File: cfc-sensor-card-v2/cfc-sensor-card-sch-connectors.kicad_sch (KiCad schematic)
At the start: 4 parts, among them J1 J-SAMTEC-TFM-120-01-L-D-RA, J3 J-SAMTEC-TFM-110-01-L-D-RA

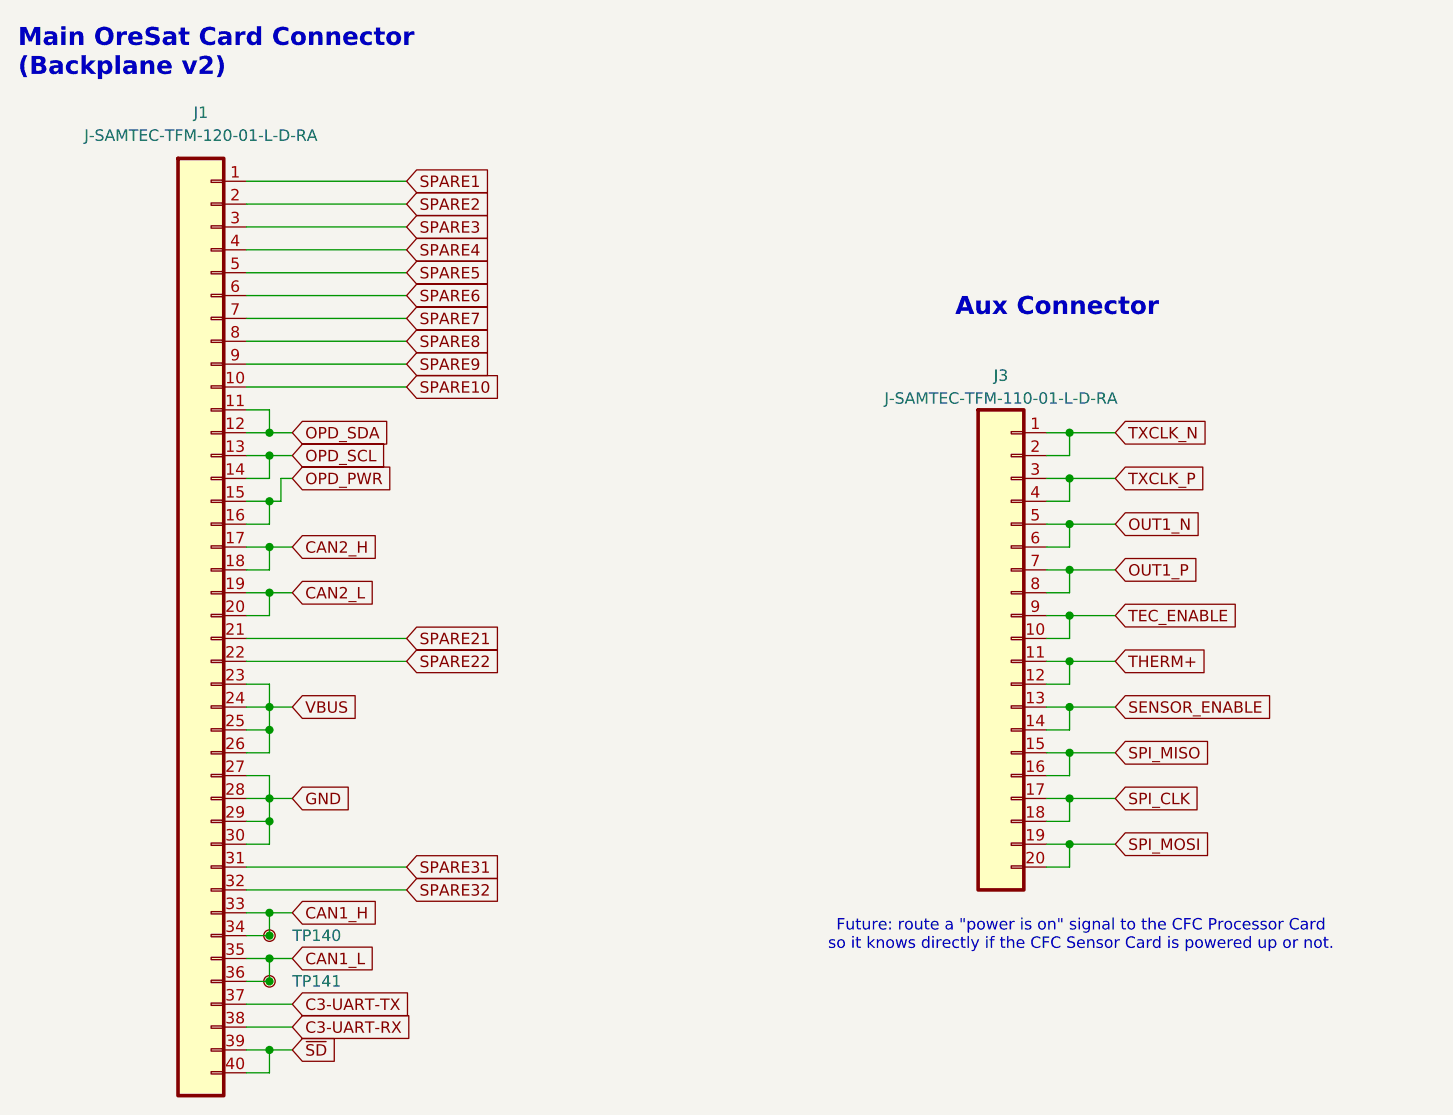
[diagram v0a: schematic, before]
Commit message: Fix and complete BOM, fix lots of little layout issue and footprint inconsistancies, and polish. Ready to go!
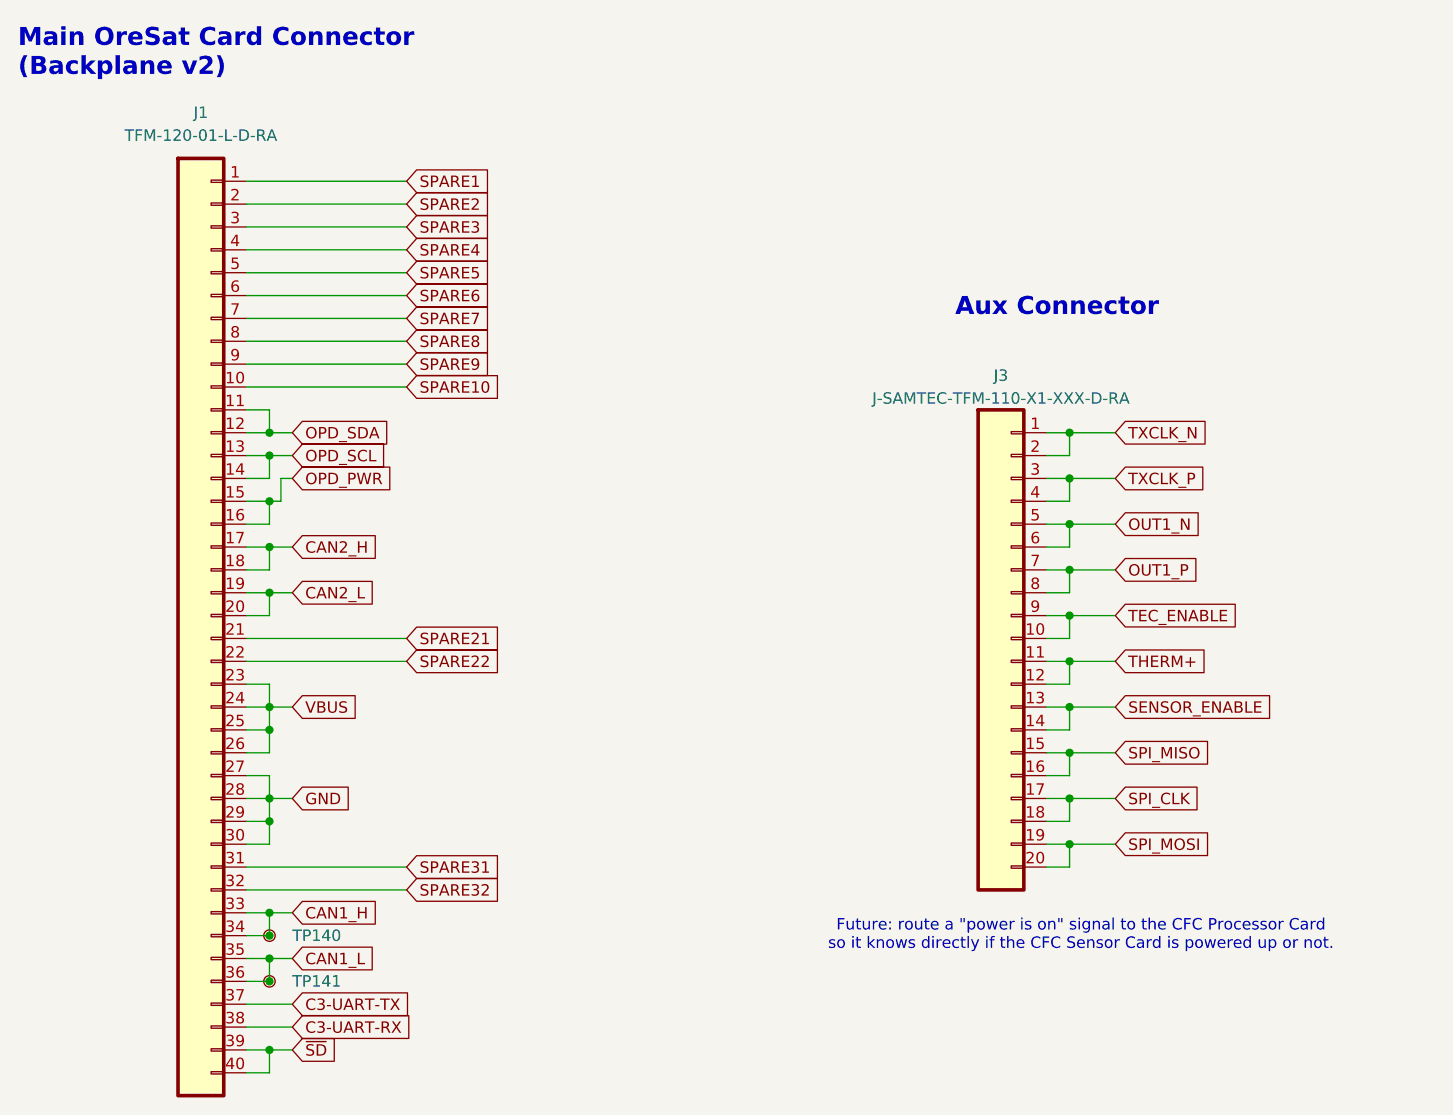
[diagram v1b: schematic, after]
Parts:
- J1: value J-SAMTEC-TFM-120-01-L-D-RA -> TFM-120-01-L-D-RA; DIS (none) -> DigiKey; DPN (none) -> SAM10145-ND; MFR (none) -> Samtec; MPN (none) -> TFM-120-01-L-D-RA
- J3: value J-SAMTEC-TFM-110-01-L-D-RA -> J-SAMTEC-TFM-110-X1-XXX-D-RA; DIS (none) -> Digikey; DPN (none) -> SAM10113-ND; MFR (none) -> Samtec; MPN (none) -> TFM-110-01-L-D-RA
- TP140, TP141: now left out of the parts list
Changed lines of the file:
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@@
 				)
 				(justify left)
-				(hide yes)
 			)
 		)
@@
 				)
 				(justify left)
-				(hide yes)
 			)
 		)
@@
 				)
 				(justify left)
-				(hide yes)
 			)
 		)
@@
 				)
 				(justify left)
-				(hide yes)
 			)
 		)
@@
 				)
 				(justify left)
-				(hide yes)
 			)
 		)
@@
 				)
 				(justify left)
-				(hide yes)
 			)
 		)
@@
 				)
 				(justify left)
-				(hide yes)
 			)
 		)
@@
 				)
 				(justify left)
-				(hide yes)
 			)
 		)
@@
 				)
 				(justify left)
-				(hide yes)
 			)
 		)
@@
 				)
 				(justify left)
-				(hide yes)
 			)
 		)
@@
 				)
 				(justify left)
-				(hide yes)
 			)
 		)
@@
 				)
 				(justify left)
-				(hide yes)
 			)
 		)
@@
 				)
 				(justify left)
-				(hide yes)
 			)
 		)
@@
 				)
 				(justify left)
-				(hide yes)
 			)
 		)
@@
 				)
 				(justify left)
-				(hide yes)
 			)
 		)
@@
 				)
 				(justify left)
-				(hide yes)
 			)
 		)
@@
 				)
 				(justify left)
-				(hide yes)
 			)
 		)
@@
 				)
 				(justify left)
-				(hide yes)
 			)
 		)
@@
 				)
 				(justify left)
-				(hide yes)
 			)
 		)
@@
 				)
 				(justify left)
-				(hide yes)
 			)
 		)
@@
 				)
 				(justify left)
-				(hide yes)
 			)
 		)
@@
 				)
 				(justify left)
-				(hide yes)
 			)
 		)
@@
 				)
 				(justify left)
-				(hide yes)
 			)
 		)
@@
 				)
 				(justify left)
-				(hide yes)
 			)
 		)
@@
 				)
 				(justify left)
-				(hide yes)
 			)
 		)
@@
 				)
 				(justify left)
-				(hide yes)
 			)
 		)
@@
 				)
 				(justify left)
-				(hide yes)
 			)
 		)
@@
 				)
 				(justify left)
-				(hide yes)
 			)
 		)
@@
 				)
 				(justify left)
-				(hide yes)
 			)
 		)
@@
 				)
 				(justify left)
-				(hide yes)
 			)
 		)
@@
 				)
 				(justify left)
-				(hide yes)
 			)
 		)
@@
 				)
 				(justify left)
-				(hide yes)
 			)
 		)
@@
 				)
 				(justify left)
-				(hide yes)
 			)
 		)
@@
 				)
 				(justify left)
-				(hide yes)
 			)
 		)
@@
 				)
 				(justify left)
-				(hide yes)
 			)
 		)
@@
 				)
 				(justify left)
-				(hide yes)
 			)
 		)
@@
 		(unit 1)
 		(exclude_from_sim no)
-		(in_bom yes)
+		(in_bom no)
 		(on_board yes)
 		(dnp no)
@@
 			)
 		)
-		(property "Description" ""
+		(property "Description" "Minimal TH Test Point (accepts scope probes and pin headers)"
 			(at 193.04 173.99 0)
+			(effects
+				(font
+					(size 1.27 1.27)
+				)
+				(hide yes)
+			)
+		)
+		(property "DIS" ""
+			(at 193.04 173.99 90)
 			(effects
 				(font
@@
 			)
 		)
-		(property "Value" "J-SAMTEC-TFM-110-01-L-D-RA"
+		(property "Value" "J-SAMTEC-TFM-110-X1-XXX-D-RA"
 			(at 274.32 114.3 0)
 			(effects
@@
 			)
 		)
-		(property "Description" "OreSat backplane connector, 2x20 RA"
+		(property "Description" "Connector Header Through Hole, Right Angle 20 position 0.050\" (1.27mm)"
+			(at 274.32 143.51 0)
+			(effects
+				(font
+					(size 1.27 1.27)
+				)
+				(hide yes)
+			)
+		)
+		(property "DIS" "Digikey"
+			(at 274.32 143.51 0)
+			(effects
+				(font
+					(size 1.27 1.27)
+				)
+				(hide yes)
+			)
+		)
+		(property "DPN" "SAM10113-ND"
+			(at 274.32 143.51 0)
+			(effects
+				(font
+					(size 1.27 1.27)
+				)
+				(hide yes)
+			)
+		)
+		(property "MFR" "Samtec"
+			(at 274.32 143.51 0)
+			(effects
+				(font
+					(size 1.27 1.27)
+				)
+				(hide yes)
+			)
+		)
+		(property "MPN" "TFM-110-01-L-D-RA "
 			(at 274.32 143.51 0)
 			(effects
@@
 			)
 		)
-		(property "Value" "J-SAMTEC-TFM-120-01-L-D-RA"
+		(property "Value" "TFM-120-01-L-D-RA"
 			(at 185.42 85.09 0)
 			(effects
@@
 			)
 		)
-		(property "Description" "OreSat backplane connector, 2x20 RA"
+		(property "Description" "Connector Header Through Hole, Right Angle 40 position 0.050\" (1.27mm)"
+			(at 185.42 138.43 0)
+			(effects
+				(font
+					(size 1.27 1.27)
+				)
+				(hide yes)
+			)
+		)
+		(property "DIS" "DigiKey"
+			(at 185.42 138.43 0)
+			(effects
+				(font
+					(size 1.27 1.27)
+				)
+				(hide yes)
+			)
+		)
+		(property "DPN" "SAM10145-ND"
+			(at 185.42 138.43 0)
+			(effects
+				(font
+					(size 1.27 1.27)
+				)
+				(hide yes)
+			)
+		)
+		(property "MFR" "Samtec"
+			(at 185.42 138.43 0)
+			(effects
+				(font
+					(size 1.27 1.27)
+				)
+				(hide yes)
+			)
+		)
+		(property "MPN" "TFM-120-01-L-D-RA"
 			(at 185.42 138.43 0)
 			(effects
@@
 		(unit 1)
 		(exclude_from_sim no)
-		(in_bom yes)
+		(in_bom no)
 		(on_board yes)
 		(dnp no)
@@
 			)
 		)
-		(property "Description" ""
+		(property "Description" "Minimal TH Test Point (accepts scope probes and pin headers)"
 			(at 193.04 179.07 0)
 			(effects
 				(font
+					(size 1.27 1.27)
+				)
+				(hide yes)
+			)
+		)
+		(property "DIS" ""
+			(at 193.04 179.07 90)
+			(effects
+				(font
